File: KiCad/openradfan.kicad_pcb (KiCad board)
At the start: 2 copper layers, 65 x 70 mm, 47 parts, among them CN1 DB141V-2.54-3P, CN2 DB141V-2.54-3P, J1 Fan_CPU_4pin, J2 Fan_CPU_4pin, J3 Fan_CPU_4pin, J4 Fan_CPU_4pin, J5 Fan_CPU_4pin, J6 Fan_CPU_4pin, J7 Fan_CPU_4pin, J8 Fan_CPU_4pin, Q1 AO3401A_C347476, U1 74AHCT125, U2 AP63205WU, U3 BTS462TATMA1

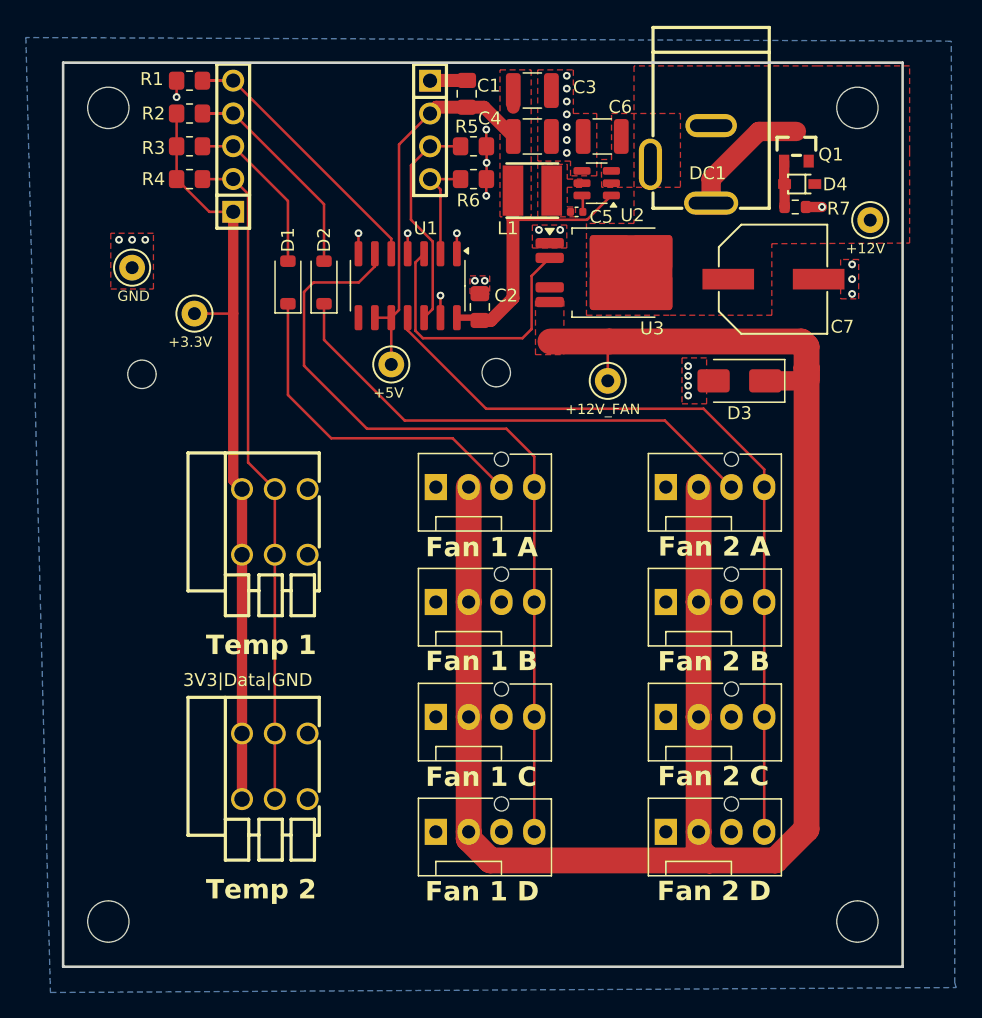
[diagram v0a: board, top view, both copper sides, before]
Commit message: Included safety components
Include reverse voltage protection, transient overvoltage protection & a resettable fuse
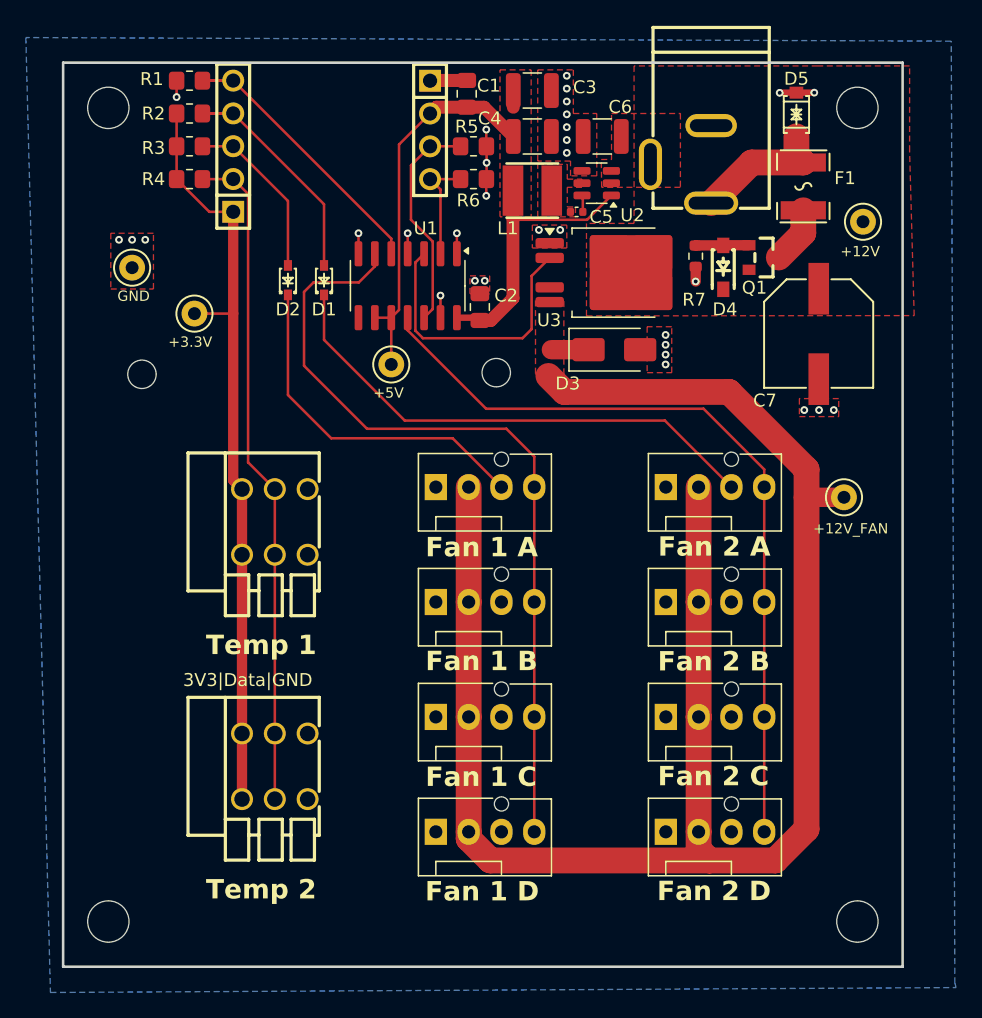
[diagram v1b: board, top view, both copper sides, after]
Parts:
- added D5: SMF14CA_C1851346, easyeda2kicad:SOD-123_L2.8-W1.8-LS3.7-BI, F.Cu at (99.4, 65.1)
- added F1: SMD1812B260TF/16, easyeda2kicad:F1812, F.Cu at (99.9, 70.7)
- D1, D2: value 1N4148W -> BAT54WS_C7502694; footprint Diode_SMD:D_SOD-123 -> easyeda2kicad:SOD-323_L1.7-W1.3-LS2.6-RD-1
- D4: value MM3Z10VT1G -> MMSZ4696T1G; footprint easyeda2kicad:SOD-323_L1.8-W1.3-LS2.5-RD -> easyeda2kicad:SOD-123_L2.7-W1.6-LS3.7-RD-1
- moved TP4 20.4 mm to (103.0, 94.7)
- moved D3 9.98 mm to (85.3, 83.3), turned to 0 degrees
- moved Q1 8.97 mm to (96.8, 76.2), turned to 180 degrees
- moved D4 8.75 mm to (93.7, 76.9), turned to 90 degrees
- moved R7 8.60 mm to (91.6, 76.1), turned to -90 degrees
- moved C7 5.50 mm to (101.1, 82.1), turned to -90 degrees
- moved D2 2.80 mm to (60.0, 77.9)
- moved D1 2.80 mm to (62.8, 77.9)
- moved TP5 0.57 mm to (104.5, 73.4)
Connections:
- D1 pad 2: GPIO_Tacho_2 -> GPIO_Tacho_1
- D2 pad 2: GPIO_Tacho_1 -> GPIO_Tacho_2
- J1 pad 3: Net-(D1-K) -> Net-(D2-K)
- J5 pad 3: Net-(D2-K) -> Net-(D1-K)
- Q1 pad 3: +12V_In -> Net-(Q1-D)
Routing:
- net Net-(D1-K): track 26.5 -> 39.7 mm
- net Net-(D2-K): track 39.1 -> 27.2 mm
- net +12V_FAN: track 149.0 -> 141.0 mm
- net Net-(Q1-D): track 0.00 -> 4.44 mm
- net GND: track 19.8 -> 22.4 mm, vias 30 -> 32
- net +12V_In: track 11.1 -> 11.8 mm
- net Net-(D4-A): track 3.52 -> 4.14 mm
